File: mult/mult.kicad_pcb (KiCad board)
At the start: 2 copper layers, 20 x 108 mm, 80 parts, among them J1 Eurorack_Power, J10 Eurorack_Mono_Jack, J11 Eurorack_Mono_Jack, J12 Eurorack_Mono_Jack_No_S, J13 Eurorack_Mono_Jack_No_S, J14 Eurorack_Mono_Jack, J15 Eurorack_Mono_Jack, J16 Eurorack_Mono_Jack_No_S, J17 Eurorack_Mono_Jack_No_S, J2 Eurorack_Mono_Jack, J3 Eurorack_Mono_Jack, J4 Eurorack_Mono_Jack_No_S, J5 Eurorack_Mono_Jack_No_S, J6 Eurorack_Mono_Jack, J7 Eurorack_Mono_Jack, J8 Eurorack_Mono_Jack_No_S, J9 Eurorack_Mono_Jack_No_S, U1 OPA4197xPW, U2 OPA4197xPW, U3 OPA4197xPW, U4 OPA4197xPW, U5 LM324

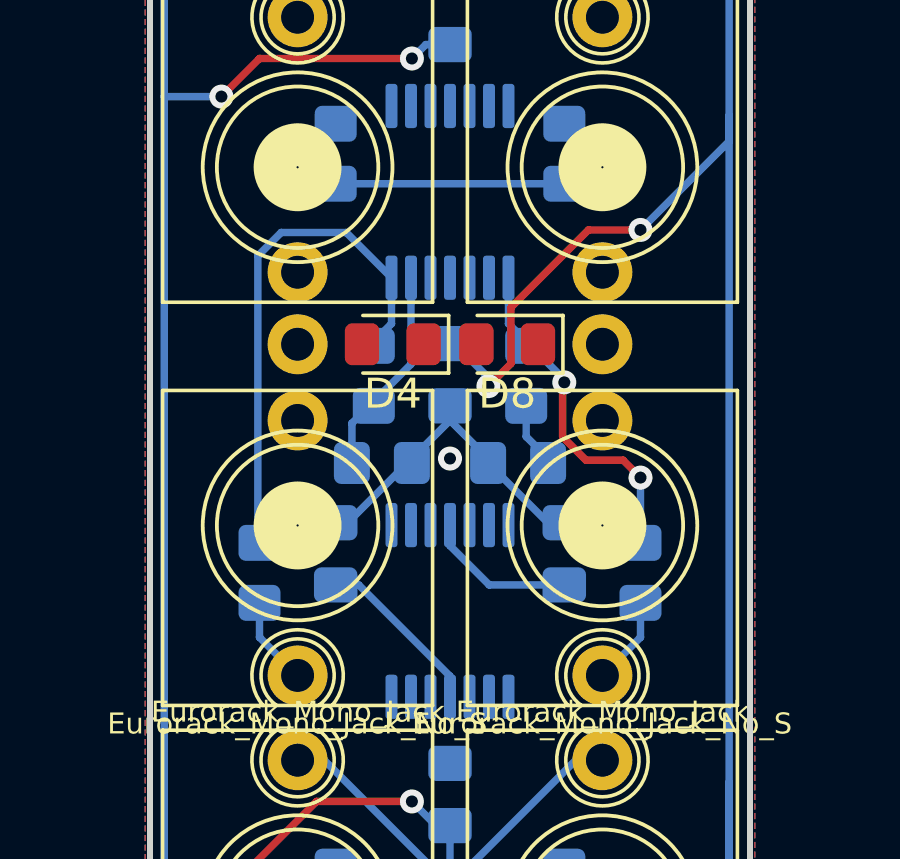
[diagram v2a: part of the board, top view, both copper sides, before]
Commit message: mult: Reorder channel schematic to match layout
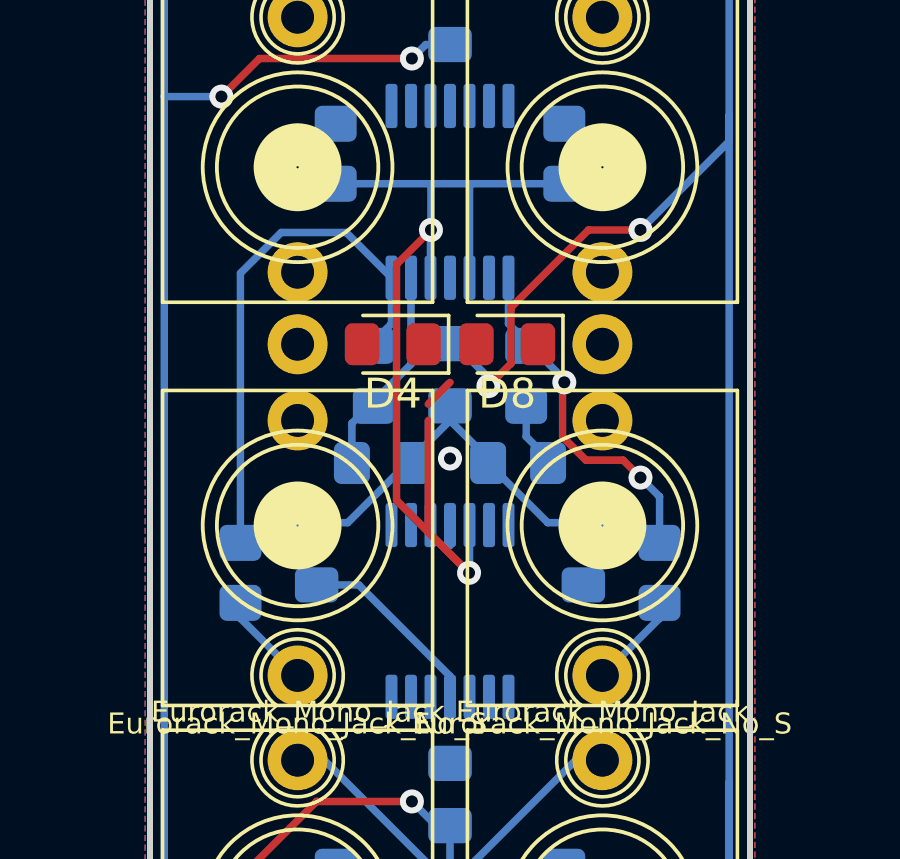
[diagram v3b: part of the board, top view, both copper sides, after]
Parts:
- moved R27 0.64 mm to (3.17, 53.3)
- moved C11 0.63 mm to (14.6, 52.7)
- moved C12 0.63 mm to (5.71, 52.7)
- moved R28 0.63 mm to (17.1, 53.3)
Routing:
- net /channel 2/average(a,b): track 7.62 -> 35.1 mm, vias 0 -> 2
- net VCC: track 128.6 -> 124.2 mm
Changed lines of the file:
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@@
   )
   (footprint "Capacitor_SMD:C_0805_2012Metric_Pad1.18x1.45mm_HandSolder" (layer "B.Cu")
-    (at 13.97 52.705 90)
+    (at 14.605 52.705 90)
     (descr "Capacitor SMD 0805 (2012 Metric), square (rectangular) end terminal, IPC_7351 nominal with elongated pad for handsoldering. (Body size source: IPC-SM-782 page 76, https://www.pcb-3d.com/wordpress/wp-content/uploads/ipc-sm-782a_amendment_1_and_2.pdf, https://docs.google.com/spreadsheets/d/1BsfQQcO9C6DZCsRaXUlFlo91Tg2WpOkGARC1WS5S8t0/edit?usp=sharing), generated with kicad-footprint-generator")
     (tags "capacitor handsolder")
@@
   )
   (footprint "Capacitor_SMD:C_0805_2012Metric_Pad1.18x1.45mm_HandSolder" (layer "B.Cu")
-    (at 6.35 52.705 90)
+    (at 5.715 52.705 90)
     (descr "Capacitor SMD 0805 (2012 Metric), square (rectangular) end terminal, IPC_7351 nominal with elongated pad for handsoldering. (Body size source: IPC-SM-782 page 76, https://www.pcb-3d.com/wordpress/wp-content/uploads/ipc-sm-782a_amendment_1_and_2.pdf, https://docs.google.com/spreadsheets/d/1BsfQQcO9C6DZCsRaXUlFlo91Tg2WpOkGARC1WS5S8t0/edit?usp=sharing), generated with kicad-footprint-generator")
     (tags "capacitor handsolder")
@@
   )
   (footprint "Resistor_SMD:R_0805_2012Metric_Pad1.20x1.40mm_HandSolder" (layer "B.Cu")
-    (at 3.81 53.34 -90)
+    (at 3.175 53.34 -90)
     (descr "Resistor SMD 0805 (2012 Metric), square (rectangular) end terminal, IPC_7351 nominal with elongated pad for handsoldering. (Body size source: IPC-SM-782 page 72, https://www.pcb-3d.com/wordpress/wp-content/uploads/ipc-sm-782a_amendment_1_and_2.pdf), generated with kicad-footprint-generator")
     (tags "resistor handsolder")
@@
   )
   (footprint "Resistor_SMD:R_0805_2012Metric_Pad1.20x1.40mm_HandSolder" (layer "B.Cu")
-    (at 16.51 53.34 -90)
+    (at 17.145 53.34 -90)
     (descr "Resistor SMD 0805 (2012 Metric), square (rectangular) end terminal, IPC_7351 nominal with elongated pad for handsoldering. (Body size source: IPC-SM-782 page 72, https://www.pcb-3d.com/wordpress/wp-content/uploads/ipc-sm-782a_amendment_1_and_2.pdf), generated with kicad-footprint-generator")
     (tags "resistor handsolder")
@@
   (segment (start 1.905 16.7425) (end 0.635 18.0125) (width 0.25) (layer "B.Cu") (net 1))
   (segment (start 10.16 63.8125) (end 10.16 61.765) (width 0.25) (layer "B.Cu") (net 1))
-  (segment (start 11.466459 53.7425) (end 13.97 53.7425) (width 0.25) (layer "B.Cu") (net 1))
   (segment (start 1.905 16.1075) (end 1.905 15.24) (width 0.25) (layer "B.Cu") (net 1))
-  (segment (start 10.16 52.436041) (end 11.466459 53.7425) (width 0.25) (layer "B.Cu") (net 1))
   (segment (start 9.355 35.73) (end 8.89 36.195) (width 0.25) (layer "B.Cu") (net 1))
   (segment (start 2.54 37.465) (end 0.635 37.465) (width 0.25) (layer "B.Cu") (net 1))
@@
   (segment (start 15.24 31.995) (end 13.215 31.995) (width 0.25) (layer "B.Cu") (net 10))
   (segment (start 13.215 31.995) (end 12.7 31.48) (width 0.25) (layer "B.Cu") (net 10))
-  (segment (start 3.81 54.34) (end 3.81 55.49) (width 0.25) (layer "B.Cu") (net 14))
-  (segment (start 3.81 55.49) (end 5.08 56.76) (width 0.25) (layer "B.Cu") (net 14))
-  (segment (start 15.24 56.76) (end 16.51 55.49) (width 0.25) (layer "B.Cu") (net 16))
-  (segment (start 16.51 55.49) (end 16.51 54.34) (width 0.25) (layer "B.Cu") (net 16))
+  (segment (start 3.175 54.34) (end 3.175 54.855) (width 0.25) (layer "B.Cu") (net 14))
+  (segment (start 3.175 54.855) (end 5.08 56.76) (width 0.25) (layer "B.Cu") (net 14))
+  (segment (start 17.145 54.34) (end 17.145 54.855) (width 0.25) (layer "B.Cu") (net 16))
+  (segment (start 17.145 54.855) (end 15.24 56.76) (width 0.25) (layer "B.Cu") (net 16))
   (segment (start 5.08 59.585) (end 5.971041 59.585) (width 0.25) (layer "B.Cu") (net 18))
   (segment (start 5.971041 59.585) (end 9.51 63.123959) (width 0.25) (layer "B.Cu") (net 18))
@@
   (segment (start 12.11 20.0075) (end 13.335 21.2325) (width 0.25) (layer "B.Cu") (net 36))
   (segment (start 13.335 22.13) (end 13.335 21.2325) (width 0.25) (layer "B.Cu") (net 36))
-  (segment (start 6.35 40.37) (end 13.97 40.37) (width 0.25) (layer "B.Cu") (net 38))
+  (segment (start 9.435 51.98) (end 9.435 48.26) (width 0.25) (layer "F.Cu") (net 38))
+  (segment (start 10.795 53.34) (end 9.435 51.98) (width 0.25) (layer "F.Cu") (net 38))
+  (segment (start 8.38 43.055) (end 9.525 41.91) (width 0.25) (layer "F.Cu") (net 38))
+  (segment (start 8.38 50.925) (end 8.38 43.055) (width 0.25) (layer "F.Cu") (net 38))
+  (segment (start 10.795 53.34) (end 8.38 50.925) (width 0.25) (layer "F.Cu") (net 38))
+  (segment (start 9.435 47.715) (end 10.16 46.99) (width 0.25) (layer "F.Cu") (net 38))
+  (via (at 9.525 41.91) (size 0.8) (drill 0.4) (layers "F.Cu" "B.Cu") (net 38))
+  (via (at 10.795 53.34) (size 0.8) (drill 0.4) (layers "F.Cu" "B.Cu") (net 38))
+  (segment (start 10.81 53.325) (end 10.795 53.34) (width 0.25) (layer "B.Cu") (net 38))
+  (segment (start 6.35 40.37) (end 9.525 40.37) (width 0.25) (layer "B.Cu") (net 38))
+  (segment (start 10.81 43.5025) (end 10.81 40.385) (width 0.25) (layer "B.Cu") (net 38))
+  (segment (start 9.525 41.91) (end 9.525 40.37) (width 0.25) (layer "B.Cu") (net 38))
+  (segment (start 9.51 43.5025) (end 9.51 41.925) (width 0.25) (layer "B.Cu") (net 38))
+  (segment (start 10.795 40.37) (end 13.97 40.37) (width 0.25) (layer "B.Cu") (net 38))
+  (segment (start 9.525 40.37) (end 10.795 40.37) (width 0.25) (layer "B.Cu") (net 38))
+  (segment (start 10.81 40.385) (end 10.795 40.37) (width 0.25) (layer "B.Cu") (net 38))
+  (segment (start 10.81 51.7475) (end 10.81 53.325) (width 0.25) (layer "B.Cu") (net 38))
+  (segment (start 9.51 41.925) (end 9.525 41.91) (width 0.25) (layer "B.Cu") (net 38))
   (segment (start 12.7 47.625) (end 12.7 48.8) (width 0.25) (layer "B.Cu") (net 40))
   (segment (start 12.7 48.8) (end 13.43 49.53) (width 0.25) (layer "B.Cu") (net 40))
-  (segment (start 3.755 42.771167) (end 4.531167 41.995) (width 0.25) (layer "B.Cu") (net 41))
+  (segment (start 3.175 52.34) (end 3.175 43.351167) (width 0.25) (layer "B.Cu") (net 41))
+  (segment (start 3.175 43.351167) (end 4.531167 41.995) (width 0.25) (layer "B.Cu") (net 41))
   (segment (start 8.21 45.035) (end 7.62 45.625) (width 0.25) (layer "B.Cu") (net 41))
-  (segment (start 3.755 52.285) (end 3.755 42.771167) (width 0.25) (layer "B.Cu") (net 41))
   (segment (start 4.531167 41.995) (end 6.7025 41.995) (width 0.25) (layer "B.Cu") (net 41))
   (segment (start 6.7025 41.995) (end 8.21 43.5025) (width 0.25) (layer "B.Cu") (net 41))
@@
   (via (at 13.97 46.99) (size 0.8) (drill 0.4) (layers "F.Cu" "B.Cu") (net 43))
   (via (at 16.51 50.165) (size 0.8) (drill 0.4) (layers "F.Cu" "B.Cu") (net 43))
-  (segment (start 16.51 50.165) (end 16.51 52.34) (width 0.25) (layer "B.Cu") (net 43))
+  (segment (start 17.145 52.34) (end 17.145 50.8) (width 0.25) (layer "B.Cu") (net 43))
   (segment (start 13.97 46.895) (end 12.7 45.625) (width 0.25) (layer "B.Cu") (net 43))
+  (segment (start 17.145 50.8) (end 16.51 50.165) (width 0.25) (layer "B.Cu") (net 43))
   (segment (start 12.11 45.035) (end 12.7 45.625) (width 0.25) (layer "B.Cu") (net 43))
   (segment (start 12.11 43.5025) (end 12.11 45.035) (width 0.25) (layer "B.Cu") (net 43))

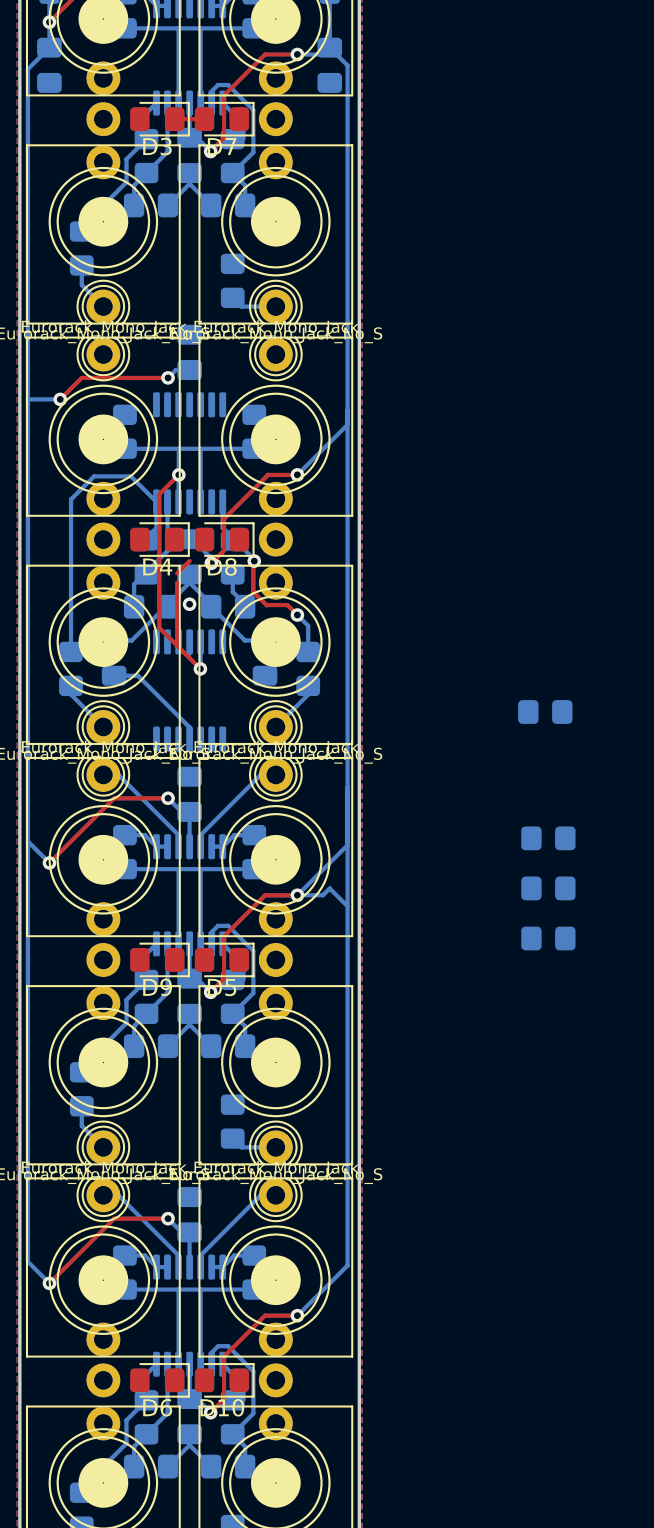
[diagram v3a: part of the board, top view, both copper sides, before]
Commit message: mult: Remove LEDs, add A-B output
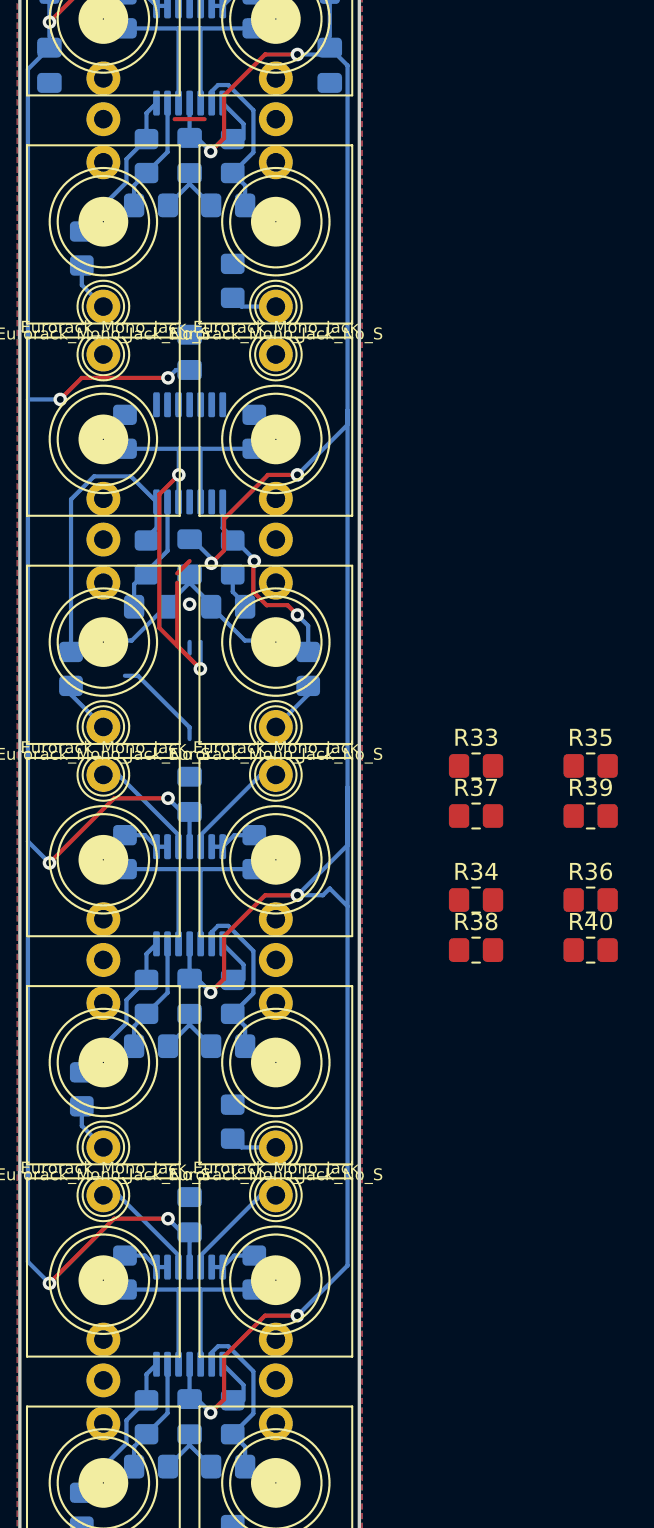
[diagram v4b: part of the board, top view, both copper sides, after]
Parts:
- removed C11, C12: 100nF, Capacitor_SMD:C_0805_2012Metric_Pad1.18x1.45mm_HandSolder
- removed D10, D3, D4, D5, D6, D7, D8, D9: LED, LED_SMD:LED_0805_2012Metric_Pad1.15x1.40mm_HandSolder
- removed U5: LM324, Package_SO:TSSOP-14_4.4x5mm_P0.65mm
- added R37: 10k, Resistor_SMD:R_0805_2012Metric_Pad1.20x1.40mm_HandSolder, F.Cu at (27.0, 62.0)
- added R38: 10k, Resistor_SMD:R_0805_2012Metric_Pad1.20x1.40mm_HandSolder, F.Cu at (27.0, 69.9)
- added R39: 10k, Resistor_SMD:R_0805_2012Metric_Pad1.20x1.40mm_HandSolder, F.Cu at (33.8, 62.0)
- added R40: 10k, Resistor_SMD:R_0805_2012Metric_Pad1.20x1.40mm_HandSolder, F.Cu at (33.8, 69.9)
- R33, R34, R35, R36: value 1k -> 10k; moved to F.Cu
- moved R35 7.63 mm to (33.8, 59.1), turned to 0 degrees
- moved R34 5.60 mm to (27.0, 67.0), turned to 0 degrees
- moved R33 5.17 mm to (27.0, 59.1), turned to 0 degrees
- moved R36 3.37 mm to (33.8, 67.0), turned to 0 degrees
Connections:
- R1 pad 1: Net-(U1A--) -> Net-(U1D-+)
- R1 pad 2: /channel 1/average(a,b) -> Net-(U1A--)
- R11 pad 1: Net-(U2C--) -> Net-(U2C-+)
- R11 pad 2: Net-(R11-Pad2) -> Net-(U2B--)
- R12 pad 2: Net-(U2C--) -> Net-(U2C-+)
- R13 pad 1: Net-(U3A--) -> Net-(U3D-+)
- R13 pad 2: /channel 3/average(a,b) -> Net-(U3A--)
- R14 pad 1: /channel 3/average(a,b) -> Net-(U3B--)
- R14 pad 2: Net-(U3B--) -> Net-(U3D-+)
- R17 pad 1: Net-(U3C--) -> Net-(U3C-+)
- R17 pad 2: Net-(R17-Pad2) -> Net-(U3B--)
- R18 pad 2: Net-(U3C--) -> Net-(U3C-+)
- R19 pad 1: Net-(U4A--) -> Net-(U4D-+)
- R19 pad 2: /channel 4/average(a,b) -> Net-(U4A--)
- R2 pad 1: /channel 1/average(a,b) -> Net-(U1B--)
- R2 pad 2: Net-(U1B--) -> Net-(U1D-+)
- R20 pad 1: /channel 4/average(a,b) -> Net-(U4B--)
- R20 pad 2: Net-(U4B--) -> Net-(U4D-+)
- R23 pad 1: Net-(U4C--) -> Net-(U4C-+)
- R23 pad 2: Net-(R23-Pad2) -> Net-(U4B--)
- R24 pad 2: Net-(U4C--) -> Net-(U4C-+)
- R28 pad 1: Net-(R11-Pad2) -> Net-(R28-Pad1)
- R30 pad 1: Net-(R17-Pad2) -> Net-(R30-Pad1)
- R32 pad 1: Net-(R23-Pad2) -> Net-(R32-Pad1)
- R33 pad 1: GND -> Net-(U1C--)
- R33 pad 2: Net-(D3-A) -> Net-(R26-Pad1)
- R34 pad 1: GND -> Net-(U2C--)
- R34 pad 2: Net-(D4-A) -> Net-(R28-Pad1)
- R35 pad 1: GND -> Net-(U3C--)
- R35 pad 2: Net-(D5-A) -> Net-(R30-Pad1)
- R36 pad 1: GND -> Net-(U4C--)
- R36 pad 2: Net-(D10-K) -> Net-(R32-Pad1)
- R5 pad 1: Net-(U1C--) -> Net-(U1C-+)
- R5 pad 2: Net-(R26-Pad1) -> Net-(U1B--)
- R6 pad 2: Net-(U1C--) -> Net-(U1C-+)
- R7 pad 1: Net-(U2A--) -> Net-(U2D-+)
- R7 pad 2: /channel 2/average(a,b) -> Net-(U2A--)
- R8 pad 1: /channel 2/average(a,b) -> Net-(U2B--)
- R8 pad 2: Net-(U2B--) -> Net-(U2D-+)
- U1 pad 10: /channel 1/average(a,b) -> Net-(U1C-+)
- U1 pad 12: /channel 1/average(a,b) -> Net-(U1D-+)
- U2 pad 10: /channel 2/average(a,b) -> Net-(U2C-+)
- U2 pad 12: /channel 2/average(a,b) -> Net-(U2D-+)
- U2 pad 8: Net-(R11-Pad2) -> Net-(R28-Pad1)
- U3 pad 10: /channel 3/average(a,b) -> Net-(U3C-+)
- U3 pad 12: /channel 3/average(a,b) -> Net-(U3D-+)
- U3 pad 8: Net-(R17-Pad2) -> Net-(R30-Pad1)
- U4 pad 10: /channel 4/average(a,b) -> Net-(U4C-+)
- U4 pad 12: /channel 4/average(a,b) -> Net-(U4D-+)
- U4 pad 8: Net-(R23-Pad2) -> Net-(R32-Pad1)
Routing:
- net (no net): track 0.00 -> 86.1 mm
- net /channel 2/average(a,b): track 35.1 -> 0.00 mm, vias 2 -> 0
- net /channel 1/average(a,b): track 16.4 -> 0.00 mm
- net /channel 4/average(a,b): track 16.4 -> 0.00 mm
- net /channel 3/average(a,b): track 16.4 -> 0.00 mm
- net Net-(U2B--): track 0.00 -> 11.7 mm, vias 0 -> 2
- net Net-(R11-Pad2): track 11.7 -> 0.00 mm, vias 2 -> 0
- net Net-(U4B--): track 2.79 -> 5.42 mm
- net Net-(R23-Pad2): track 2.63 -> 0.00 mm
- net Net-(R17-Pad2): track 2.63 -> 0.00 mm
- net Net-(U3B--): track 2.79 -> 5.42 mm
- net Net-(U2C--): track 2.21 -> 0.00 mm
- net Net-(U2C-+): track 0.00 -> 2.21 mm
- net Net-(D3-K): track 1.76 -> 0.00 mm
- net Net-(U2D-+): vias 0 -> 2

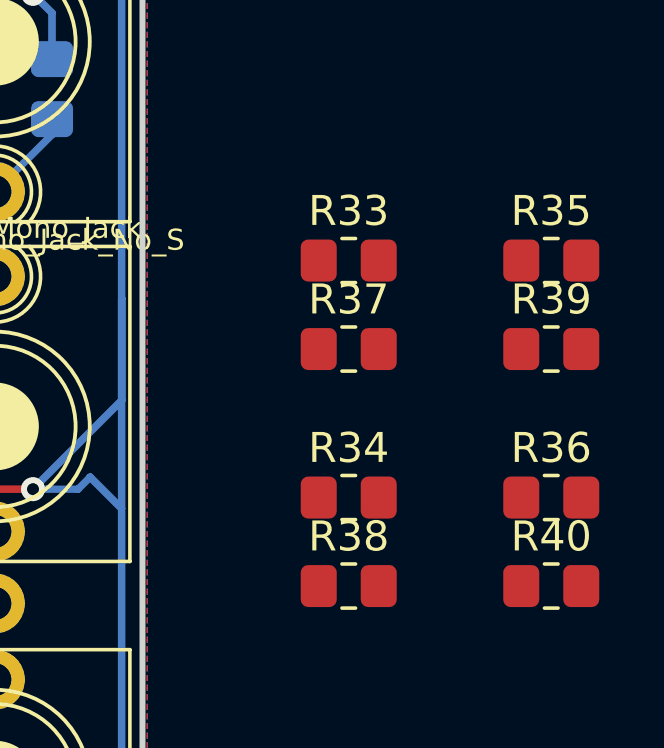
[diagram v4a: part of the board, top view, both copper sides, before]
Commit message: mult: Update resistor references
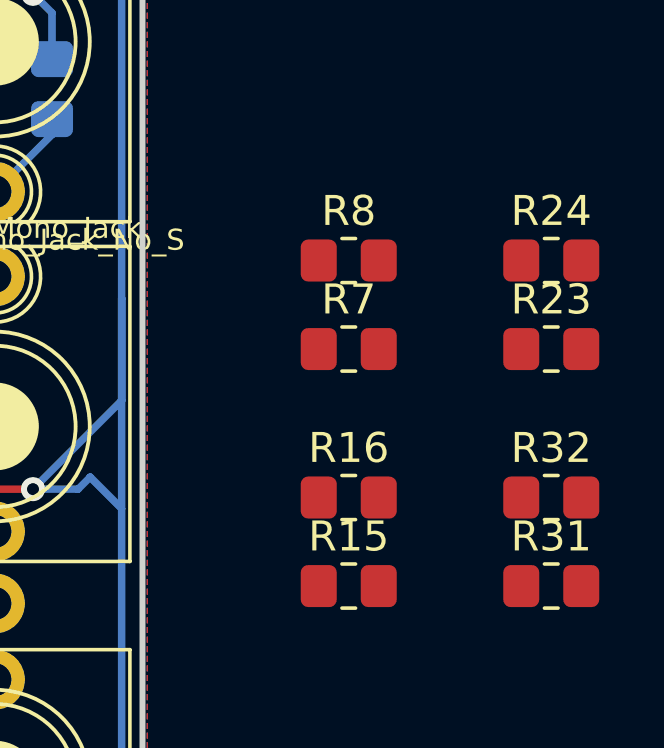
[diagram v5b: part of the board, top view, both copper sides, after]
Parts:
- renumbered R8 to R10, R9 to R11, R10 to R12, R11 to R13, R12 to R14, R38 to R15, R34 to R16, R13 to R17, R14 to R18, R15 to R19, R16 to R20, R17 to R21, R18 to R22, R39 to R23, R35 to R24, R19 to R25, R20 to R26, R21 to R27, R22 to R28, R23 to R29, R24 to R30, R40 to R31, R36 to R32, R25 to R33, R26 to R34, R27 to R35, R28 to R36, R29 to R37, R30 to R38, R31 to R39, R32 to R40, R37 to R7, R33 to R8, R7 to R9
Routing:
- net Net-(U1B--): track 2.79 -> 5.42 mm
- net Net-(R34-Pad1): track 2.63 -> 0.00 mm
